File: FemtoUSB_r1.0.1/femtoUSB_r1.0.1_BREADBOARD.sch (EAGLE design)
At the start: 33 parts, among them IC1 ATSAMD21E18A-MUT

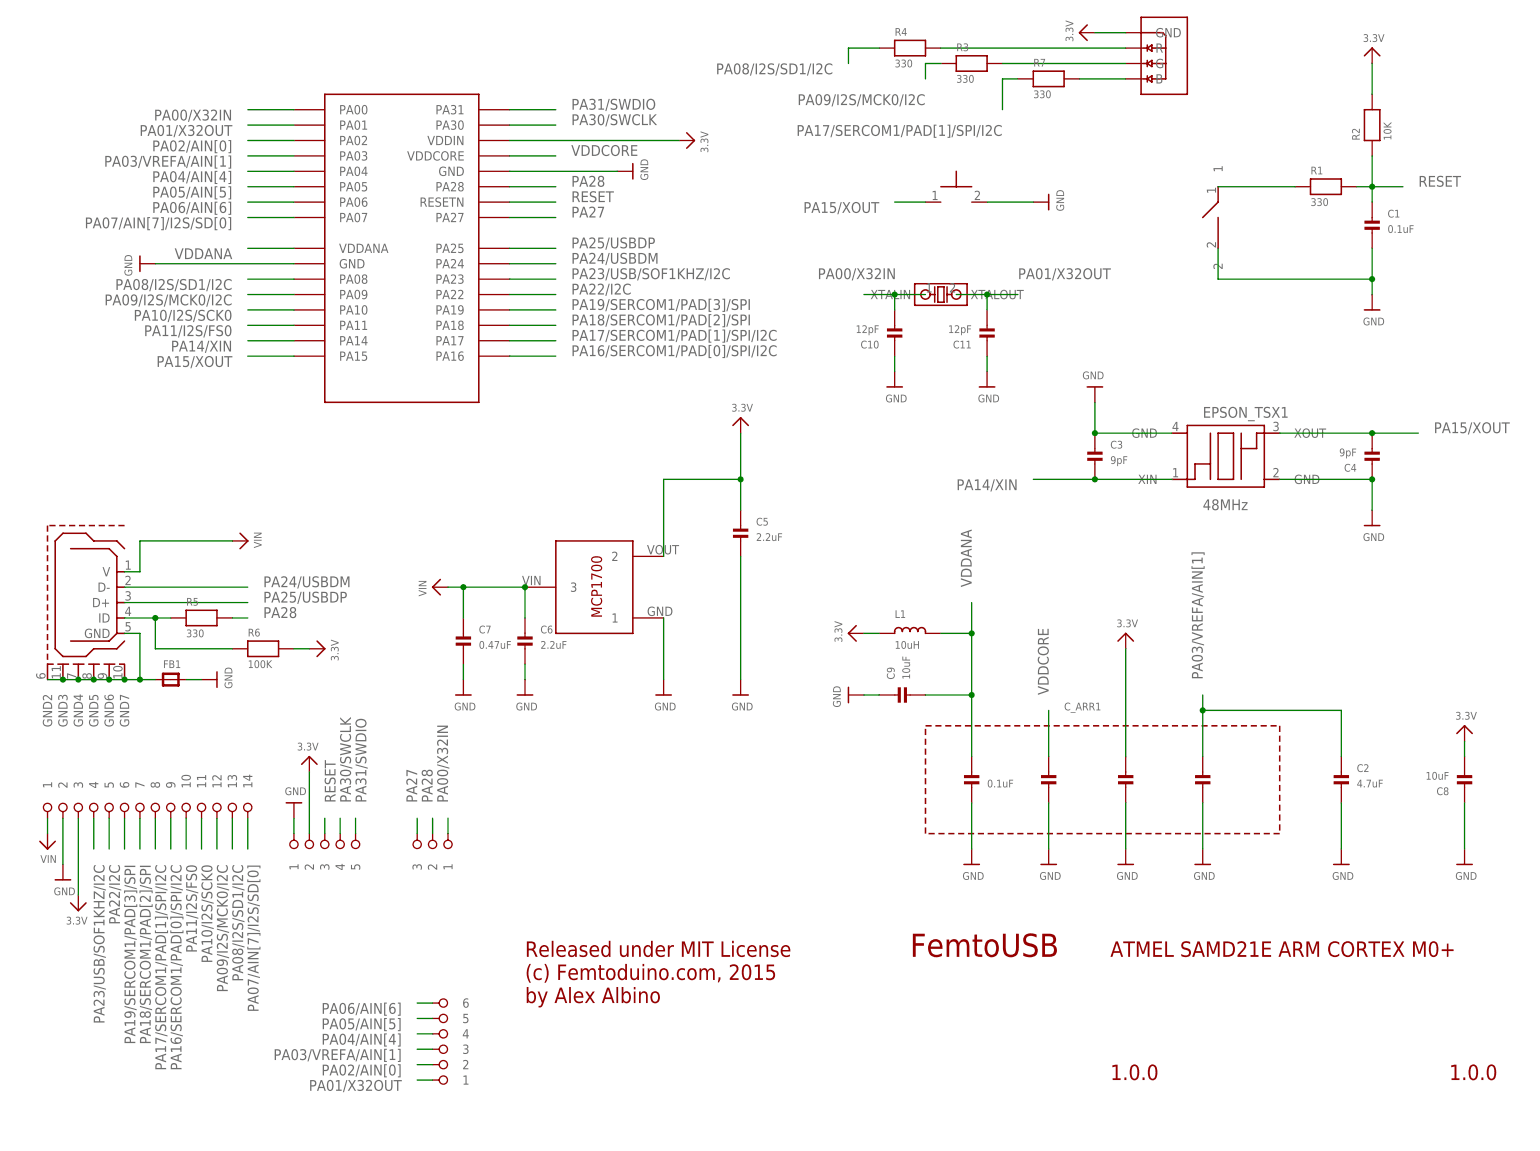
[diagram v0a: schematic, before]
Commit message: Updating breadboard version. Adjusting USB ID pin connection back to PA28 on both FemtoUSB, and FemtoUSB breadboard layout
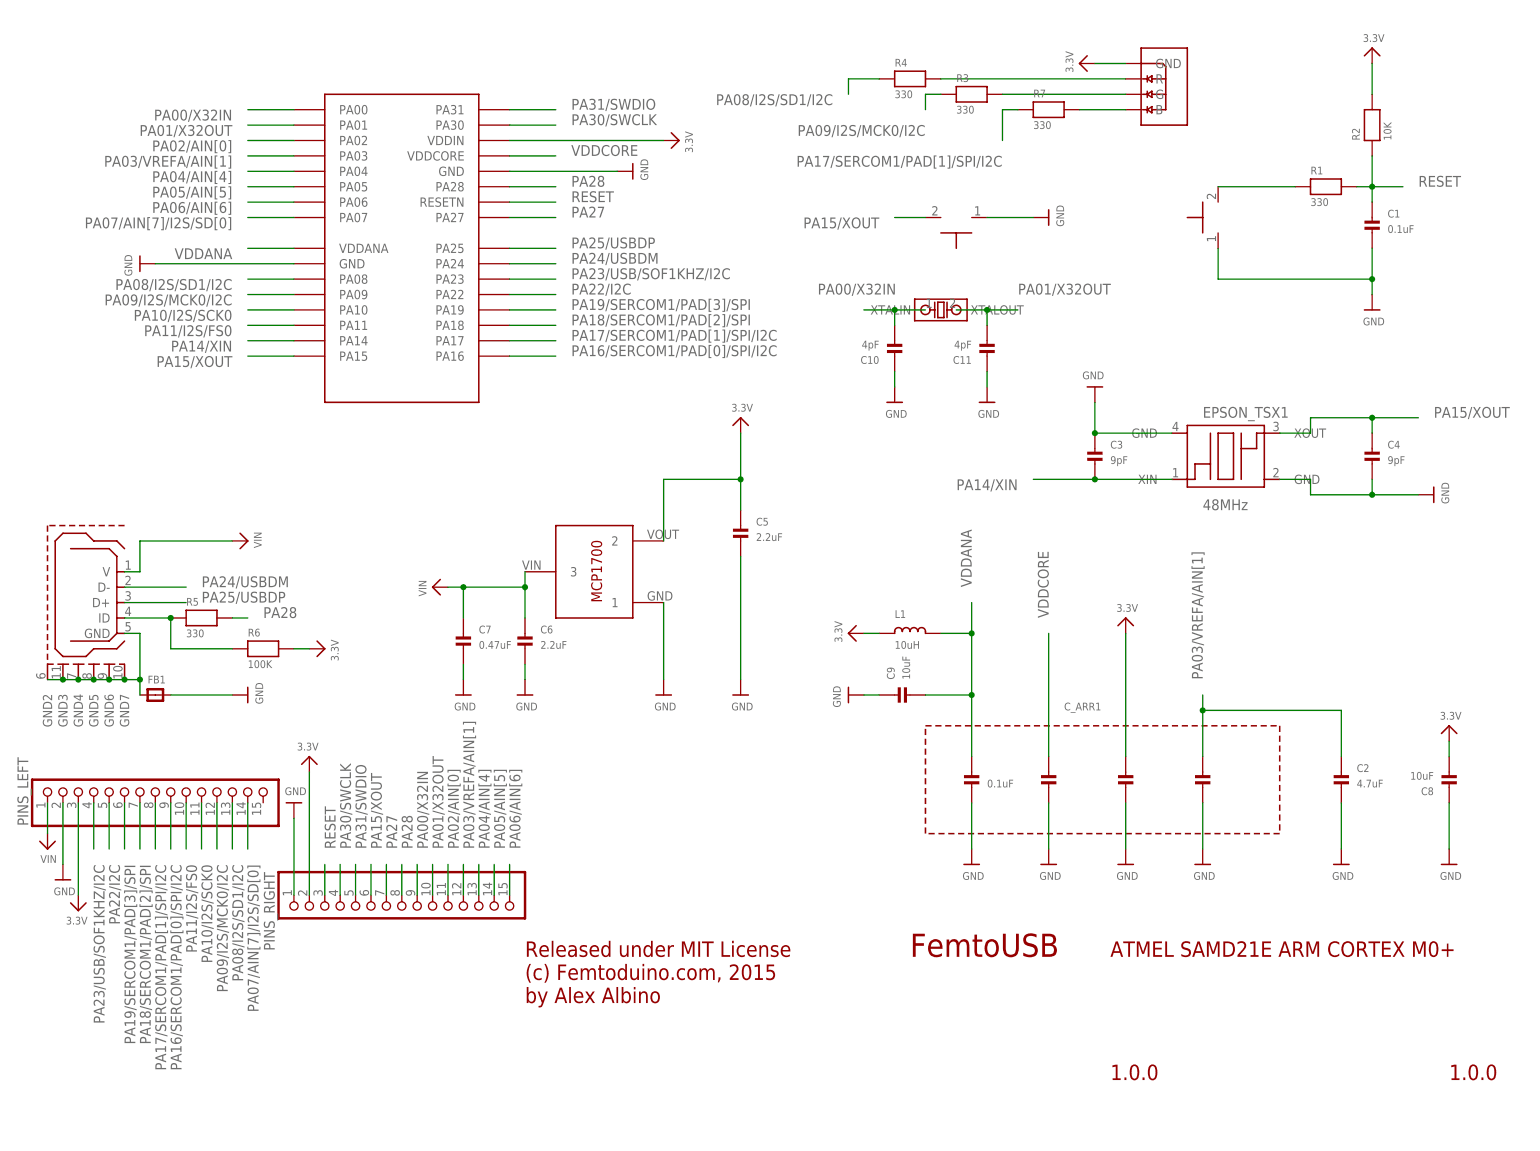
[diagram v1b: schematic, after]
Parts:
- removed SJ_RESET: OMRON B3U-300P(M), femtoduino:SPST_SMD
- removed U$12: 1X6_ROUND, pins_1.27mm_pitch:1X6_ROUND
- removed U$43: TACTILE_SWITCH_NO_GND_NO_BOSS, omron_tactile_switch:TACTILE_SWITCH_NO_GND_NO_BOSS
- removed U$6: 1X14_ROUND, pins_1.27mm_pitch:1X14_ROUND
- removed U$7: 1X3_ROUND, pins_1.27mm_pitch:1X3_ROUND
- removed U$9: 1X5_ROUND, pins_1.27mm_pitch:1X5_ROUND
- added BOOT_BTN, BOOT_BTN1: TACTILE_SWITCH_NO_GND_NO_BOSS, omron_tactile_switch:TACTILE_SWITCH_NO_GND_NO_BOSS
- added PINS_LEFT, PINS_RIGHT: (no value), microbuilder:HEADER-1X15
- C1: DIGIKEY_PART (none) -> 445-4958-1-ND
- C10, C11: value 12pF -> 4pF
- IC1: DIGIKEY_PART (none) -> ATSAMD21E18A-AU-ND
- R1: DIGIKEY_PART (none) -> 541-330JCT-ND
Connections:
- net N$32 renamed GND_RAW
- net 3.3V: now also PINS_LEFT.3, PINS_RIGHT.2; no longer U$6.3, U$9.2
- net GND: now also BOOT_BTN.1, BOOT_BTN1.1, C4.P$2, PINS_LEFT.2, PINS_RIGHT.1; no longer C4.P$1, SJ_RESET.2, U$43.2, U$6.2, U$9.1
- net N$26: now also BOOT_BTN1.2; no longer SJ_RESET.1
- net PA00/X32IN: now also PINS_RIGHT.9; no longer U$7.1
- net PA01/X32OUT: now also PINS_RIGHT.10; no longer U$12.1
- net PA02/AIN[0]: now also PINS_RIGHT.11; no longer U$12.2
- net PA03/VREFA/AIN[1]: now also PINS_RIGHT.12; no longer U$12.3
- net PA04/AIN[4]: now also PINS_RIGHT.13; no longer U$12.4
- net PA05/AIN[5]: now also PINS_RIGHT.14; no longer U$12.5
- net PA06/AIN[6]: now also PINS_RIGHT.15; no longer U$12.6
- net PA07/AIN[7]/I2S/SD[0]: now also PINS_LEFT.14; no longer U$6.14
- net PA08/I2S/SD1/I2C: now also PINS_LEFT.13; no longer U$6.13
- net PA09/I2S/MCK0/I2C: now also PINS_LEFT.12; no longer U$6.12
- net PA10/I2S/SCK0: now also PINS_LEFT.11; no longer U$6.11
- net PA11/I2S/FS0: now also PINS_LEFT.10; no longer U$6.10
- net PA15/XOUT: now also BOOT_BTN.2, C4.P$1, PINS_RIGHT.6; no longer C4.P$2, U$43.1
- net PA16/SERCOM1/PAD[0]/SPI/I2C: now also PINS_LEFT.9; no longer U$6.9
- net PA17/SERCOM1/PAD[1]/SPI/I2C: now also PINS_LEFT.8; no longer U$6.8
- net PA18/SERCOM1/PAD[2]/SPI: now also PINS_LEFT.7; no longer U$6.7
- net PA19/SERCOM1/PAD[3]/SPI: now also PINS_LEFT.6; no longer U$6.6
- net PA22/I2C: now also PINS_LEFT.5; no longer U$6.5
- net PA23/USB/SOF1KHZ/I2C: now also PINS_LEFT.4; no longer U$6.4
- net PA27: now also PINS_RIGHT.7; no longer U$7.3
- net PA28: now also PINS_RIGHT.8; no longer U$7.2
- net PA30/SWCLK: now also PINS_RIGHT.4; no longer U$9.4
- net PA31/SWDIO: now also PINS_RIGHT.5; no longer U$9.5
- net RESET: now also PINS_RIGHT.3; no longer U$9.3
- net VIN: now also PINS_LEFT.1; no longer U$6.1
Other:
- moved on the sheet: C10, C11, C4, C8, FB1, R3, R4, R7
